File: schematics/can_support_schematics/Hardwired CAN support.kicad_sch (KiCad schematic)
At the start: 35 parts, among them J1 Conn_01x05_Female, J2 Conn_01x05_Male, J3 Conn_01x05_Male, J4 Screw_Terminal_01x04, J5 Screw_Terminal_01x02, J6 Screw_Terminal_01x02, J7 Screw_Terminal_01x02, Q1 MMBF170, SW1 SW_DIP_x04, U1 SPST_POWER_RELAY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

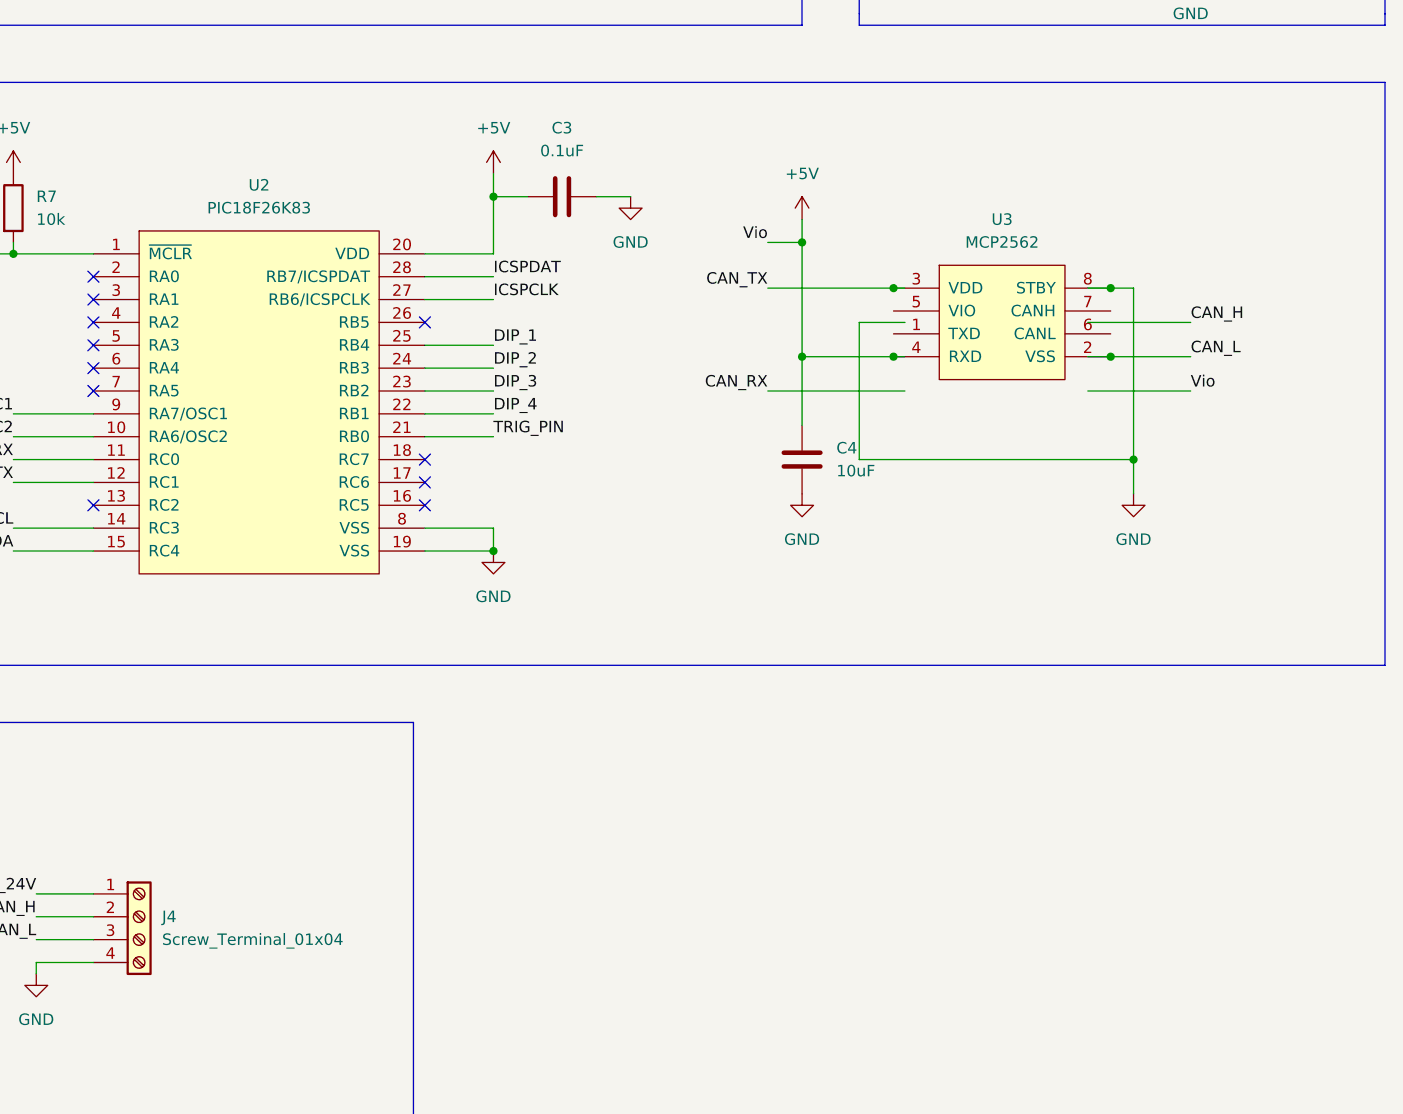
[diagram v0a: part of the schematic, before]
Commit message: Fixed CAN transceiver
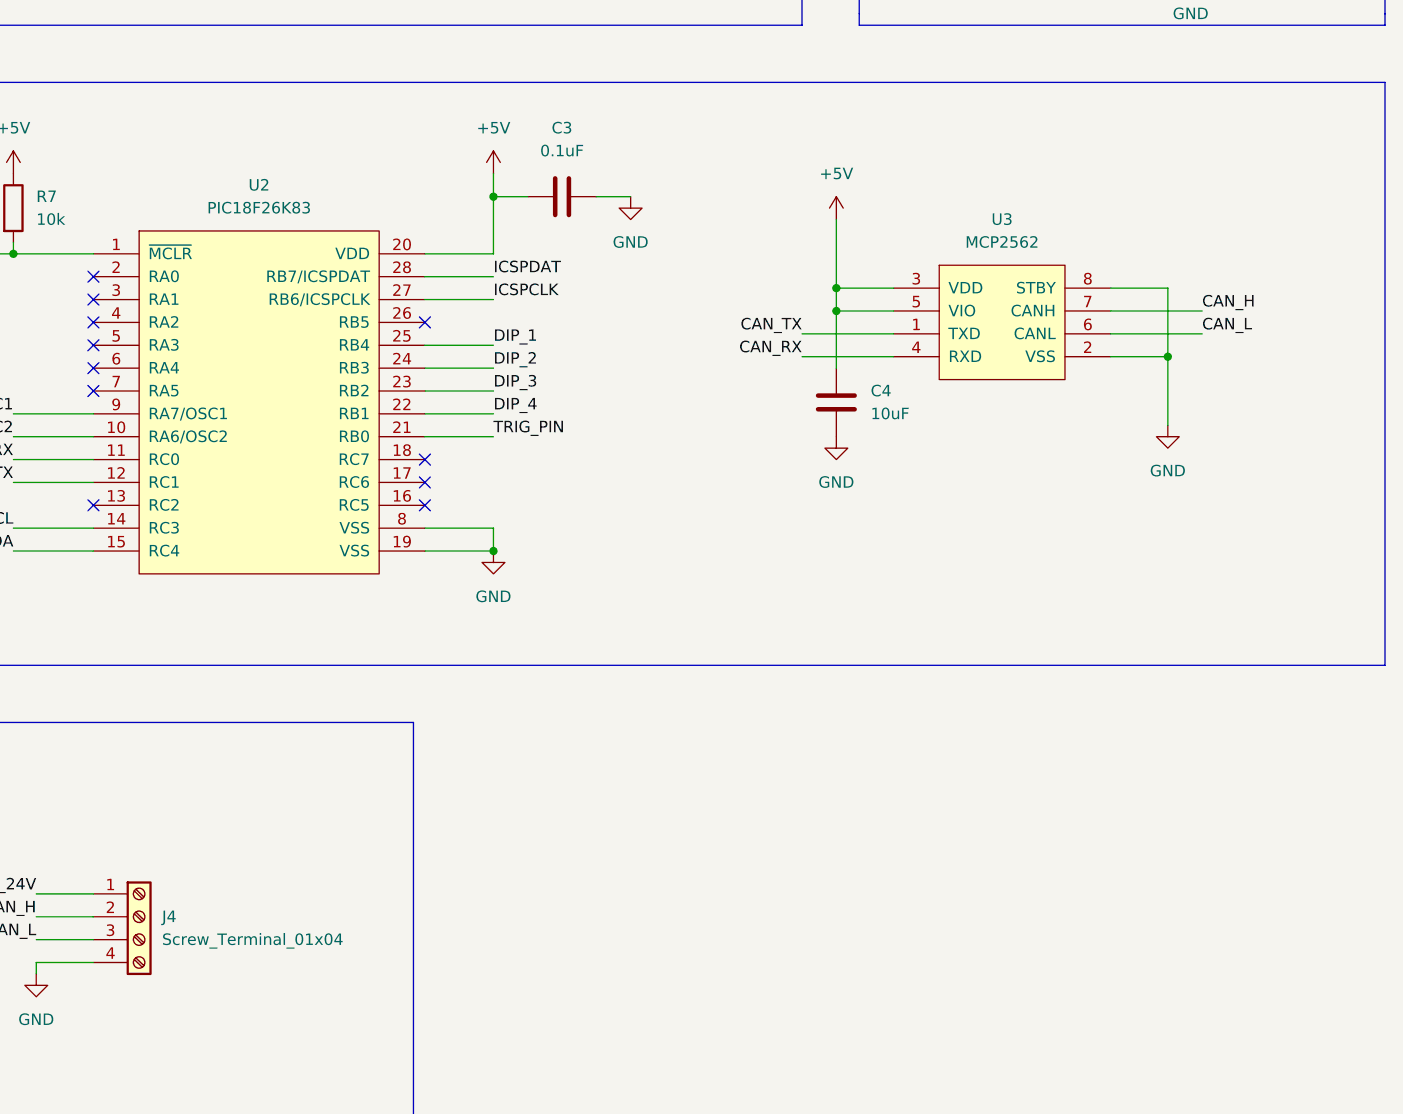
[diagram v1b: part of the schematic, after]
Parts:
- C4: footprint Capacitor_SMD:C_0805_2012Metric_Pad1.18x1.45mm_HandSolder -> (none)
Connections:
- net +5V: now also U3.3 (VDD), U3.5 (VIO); no longer U3.4 (RXD)
- net CAN_H: now also U3.7 (CANH)
- net CAN_L: now also U3.6 (CANL); no longer U3.2 (VSS)
- net CAN_RX: now also U3.4 (RXD)
- net CAN_TX: now also U3.1 (TXD); no longer U3.3 (VDD)
- net GND: now also U3.2 (VSS)

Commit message: Layout for PCB Plz Check and other updates
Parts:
- C4: footprint (none) -> Capacitor_SMD:C_0805_2012Metric_Pad1.18x1.45mm_HandSolder
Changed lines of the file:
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@@
       (effects (font (size 1.27 1.27)) (justify left))
     )
-    (property "Footprint" "" (id 2) (at 218.1352 104.14 0)
+    (property "Footprint" "Capacitor_SMD:C_0805_2012Metric_Pad1.18x1.45mm_HandSolder" (id 2) (at 218.1352 104.14 0)
       (effects (font (size 1.27 1.27)) hide)
     )
@@
     )
     (path "/d85f2563-6057-4c63-b8bd-55bd96b3561a"
-      (reference "C4") (unit 1) (value "10uF") (footprint "")
+      (reference "C4") (unit 1) (value "10uF") (footprint "Capacitor_SMD:C_0805_2012Metric_Pad1.18x1.45mm_HandSolder")
     )
     (path "/cb5f6738-8708-448f-b483-2bb4d72a4e96"

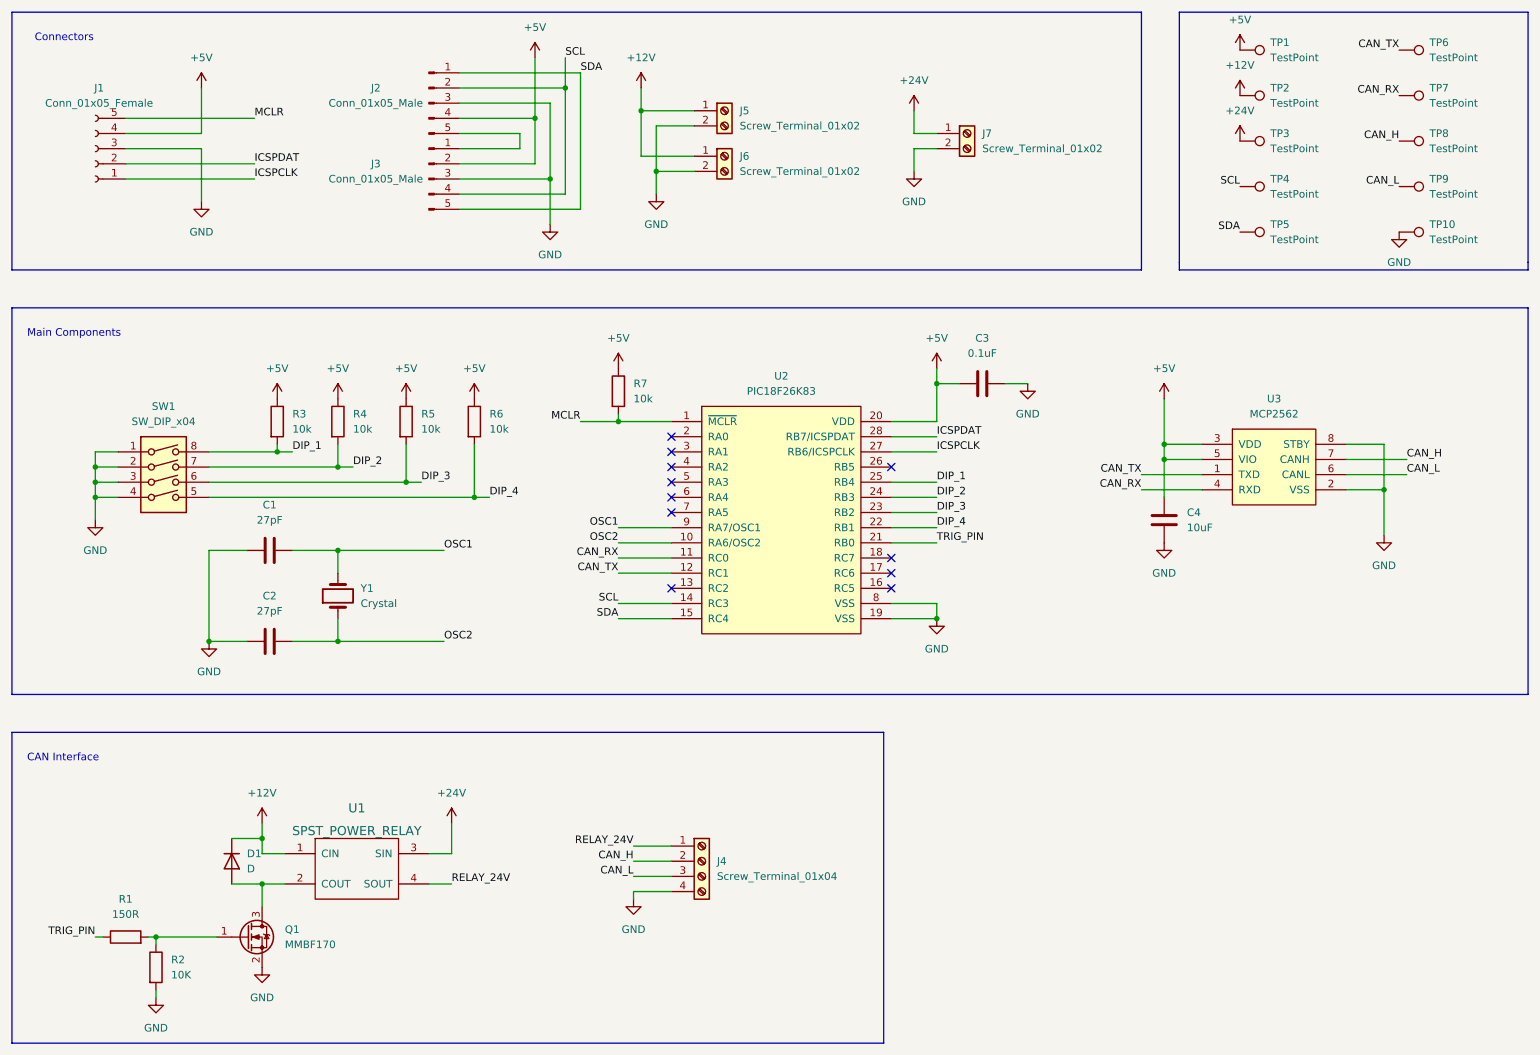
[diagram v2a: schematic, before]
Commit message: Finished routing board
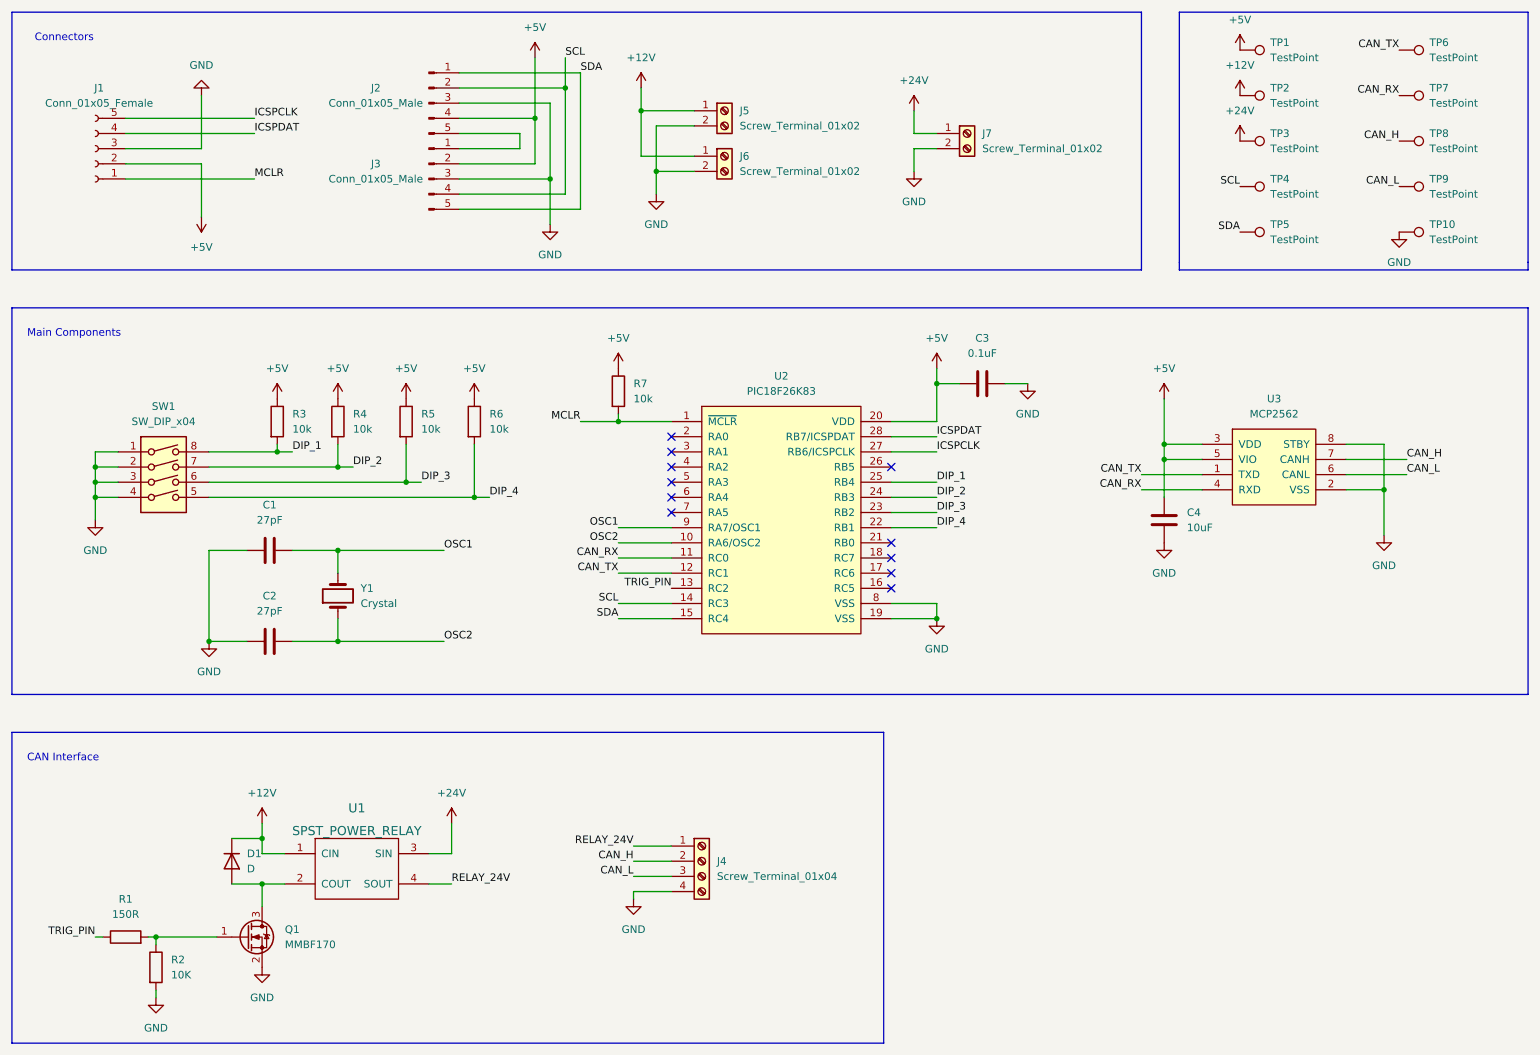
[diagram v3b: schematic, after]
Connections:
- net +5V: now also J1.2 (Pin_2); no longer J1.4 (Pin_4)
- net ICSPCLK: now also J1.5 (Pin_5); no longer J1.1 (Pin_1)
- net ICSPDAT: now also J1.4 (Pin_4); no longer J1.2 (Pin_2)
- net MCLR: now also J1.1 (Pin_1); no longer J1.5 (Pin_5)
- net TRIG_PIN: now also U2.13 (RC2); no longer U2.21 (RB0)
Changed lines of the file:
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@@
   (junction (at 101.6 96.52) (diameter 0) (color 0 0 0 0)
   )
-  (no_connect (at 134.62 111.76))
   (no_connect (at 171.45 106.68))
   (no_connect (at 171.45 111.76))
@@
   (no_connect (at 134.62 99.06))
   (no_connect (at 134.62 96.52))
+  (no_connect (at 171.45 104.14))
   (wire (pts (xy 111.76 40.64) (xy 99.06 40.64))
     (stroke (width 0) (type default) (color 0 0 0 0))
@@
     (stroke (width 0) (type default) (color 0 0 0 0))
   )
-  (wire (pts (xy 43.18 35.56) (xy 55.88 35.56))
+  (wire (pts (xy 43.18 35.56) (xy 64.77 35.56))
     (stroke (width 0) (type default) (color 0 0 0 0))
   )
@@
     (stroke (width 0) (type default) (color 0 0 0 0))
   )
+  (wire (pts (xy 55.88 29.21) (xy 55.88 38.1))
+    (stroke (width 0) (type default) (color 0 0 0 0))
+  )
   (wire (pts (xy 132.08 41.91) (xy 132.08 45.72))
     (stroke (width 0) (type default) (color 0 0 0 0))
@@
     (stroke (width 0) (type default) (color 0 0 0 0))
   )
-  (wire (pts (xy 55.88 38.1) (xy 55.88 46.99))
-    (stroke (width 0) (type default) (color 0 0 0 0))
-  )
   (wire (pts (xy 66.04 161.29) (xy 66.04 165.1))
     (stroke (width 0) (type default) (color 0 0 0 0))
@@
     (stroke (width 0) (type default) (color 0 0 0 0))
   )
-  (wire (pts (xy 55.88 27.94) (xy 55.88 35.56))
-    (stroke (width 0) (type default) (color 0 0 0 0))
-  )
   (wire (pts (xy 171.45 116.84) (xy 179.07 116.84))
     (stroke (width 0) (type default) (color 0 0 0 0))
@@
     (stroke (width 0) (type default) (color 0 0 0 0))
   )
-  (wire (pts (xy 43.18 40.64) (xy 64.77 40.64))
+  (wire (pts (xy 43.18 40.64) (xy 55.88 40.64))
     (stroke (width 0) (type default) (color 0 0 0 0))
   )
@@
     (stroke (width 0) (type default) (color 0 0 0 0))
   )
-  (wire (pts (xy 171.45 104.14) (xy 179.07 104.14))
-    (stroke (width 0) (type default) (color 0 0 0 0))
-  )
   (wire (pts (xy 171.45 88.9) (xy 179.07 88.9))
     (stroke (width 0) (type default) (color 0 0 0 0))
@@
     (stroke (width 0) (type default) (color 0 0 0 0))
   )
+  (wire (pts (xy 55.88 40.64) (xy 55.88 49.53))
+    (stroke (width 0) (type default) (color 0 0 0 0))
+  )
   (wire (pts (xy 71.12 105.41) (xy 78.74 105.41))
     (stroke (width 0) (type default) (color 0 0 0 0))
@@
     (effects (font (size 1.27 1.27)) (justify right bottom))
   )
+  (label "TRIG_PIN" (at 134.62 111.76 180)
+    (effects (font (size 1.27 1.27)) (justify right bottom))
+  )
   (label "CAN_L" (at 257.81 92.71 0)
     (effects (font (size 1.27 1.27)) (justify left bottom))
   )
-  (label "MCLR" (at 64.77 33.02 0)
-    (effects (font (size 1.27 1.27)) (justify left bottom))
-  )
-  (label "ICSPDAT" (at 64.77 40.64 0)
-    (effects (font (size 1.27 1.27)) (justify left bottom))
-  )
-  (label "TRIG_PIN" (at 179.07 104.14 0)
+  (label "MCLR" (at 64.77 43.18 0)
     (effects (font (size 1.27 1.27)) (justify left bottom))
   )
@@
     (effects (font (size 1.27 1.27)) (justify right bottom))
   )
-  (label "ICSPCLK" (at 64.77 43.18 0)
-    (effects (font (size 1.27 1.27)) (justify left bottom))
-  )
   (label "DIP_1" (at 179.07 93.98 0)
     (effects (font (size 1.27 1.27)) (justify left bottom))
@@
     (effects (font (size 1.27 1.27)) (justify right bottom))
   )
+  (label "ICSPDAT" (at 64.77 35.56 0)
+    (effects (font (size 1.27 1.27)) (justify left bottom))
+  )
   (label "DIP_4" (at 104.14 96.52 0)
     (effects (font (size 1.27 1.27)) (justify left bottom))
@@
   )
   (label "RELAY_24V" (at 97.79 161.29 0)
+    (effects (font (size 1.27 1.27)) (justify left bottom))
+  )
+  (label "ICSPCLK" (at 64.77 33.02 0)
     (effects (font (size 1.27 1.27)) (justify left bottom))
   )
@@
     (pin "1")
   )
+  (symbol (lib_id "power:GND") (at 55.88 29.21 180) (unit 1)
+    (in_bom yes) (on_board yes) (fields_autoplaced)
+    (property "Reference" "#PWR0106" (id 0) (at 55.88 22.86 0)
+      (effects (font (size 1.27 1.27)) hide)
+    )
+    (property "Value" "GND" (id 1) (at 55.88 24.13 0))
+    (property "Footprint" "" (id 2) (at 55.88 29.21 0)
+      (effects (font (size 1.27 1.27)) hide)
+    )
+    (property "Datasheet" "" (id 3) (at 55.88 29.21 0)
+      (effects (font (size 1.27 1.27)) hide)
+    )
+    (pin "1")
+  )
   (symbol (lib_id "power:+12V") (at 229.87 29.21 0) (unit 1)
     (in_bom yes) (on_board yes) (fields_autoplaced)
@@
     )
     (property "Datasheet" "" (id 3) (at 66.04 175.26 0)
-      (effects (font (size 1.27 1.27)) hide)
-    )
-    (pin "1")
-  )
-  (symbol (lib_id "power:GND") (at 55.88 46.99 0) (unit 1)
-    (in_bom yes) (on_board yes) (fields_autoplaced)
-    (property "Reference" "#PWR04" (id 0) (at 55.88 53.34 0)
-      (effects (font (size 1.27 1.27)) hide)
-    )
-    (property "Value" "GND" (id 1) (at 55.88 52.07 0))
-    (property "Footprint" "" (id 2) (at 55.88 46.99 0)
-      (effects (font (size 1.27 1.27)) hide)
-    )
-    (property "Datasheet" "" (id 3) (at 55.88 46.99 0)
       (effects (font (size 1.27 1.27)) hide)
     )
@@
     )
     (property "Datasheet" "" (id 3) (at 125.73 74.93 0)
+      (effects (font (size 1.27 1.27)) hide)
+    )
+    (pin "1")
+  )
+  (symbol (lib_id "power:+5V") (at 55.88 49.53 180) (unit 1)
+    (in_bom yes) (on_board yes) (fields_autoplaced)
+    (property "Reference" "#PWR0105" (id 0) (at 55.88 45.72 0)
+      (effects (font (size 1.27 1.27)) hide)
+    )
+    (property "Value" "+5V" (id 1) (at 55.88 54.61 0))
+    (property "Footprint" "" (id 2) (at 55.88 49.53 0)
+      (effects (font (size 1.27 1.27)) hide)
+    )
+    (property "Datasheet" "" (id 3) (at 55.88 49.53 0)
       (effects (font (size 1.27 1.27)) hide)
     )
@@
     (pin "1")
   )
-  (symbol (lib_id "power:+5V") (at 55.88 27.94 0) (unit 1)
-    (in_bom yes) (on_board yes) (fields_autoplaced)
-    (property "Reference" "#PWR03" (id 0) (at 55.88 31.75 0)
-      (effects (font (size 1.27 1.27)) hide)
-    )
-    (property "Value" "+5V" (id 1) (at 55.88 22.86 0))
-    (property "Footprint" "" (id 2) (at 55.88 27.94 0)
-      (effects (font (size 1.27 1.27)) hide)
-    )
-    (property "Datasheet" "" (id 3) (at 55.88 27.94 0)
-      (effects (font (size 1.27 1.27)) hide)
-    )
-    (pin "1")
-  )
   (symbol (lib_id "Connector:TestPoint") (at 256.54 29.21 270) (unit 1)
     (in_bom yes) (on_board yes) (fields_autoplaced)
@@
       (reference "#PWR02") (unit 1) (value "+5V") (footprint "")
     )
-    (path "/fc3e498d-d0cd-4c1a-a2fe-632568988592"
-      (reference "#PWR03") (unit 1) (value "+5V") (footprint "")
-    )
-    (path "/7d654e39-30f5-4364-b45a-95a72d3c3ee4"
-      (reference "#PWR04") (unit 1) (value "GND") (footprint "")
-    )
     (path "/705e8294-3269-44a7-a117-43cc65252d68"
       (reference "#PWR05") (unit 1) (value "GND") (footprint "")
@@
       (reference "#PWR0104") (unit 1) (value "+24V") (footprint "")
     )
+    (path "/c91b8104-1c96-4bf2-b6fb-8bdf8adbf6c6"
+      (reference "#PWR0105") (unit 1) (value "+5V") (footprint "")
+    )
+    (path "/6ba02eba-914c-45a1-b69c-35b19e165048"
+      (reference "#PWR0106") (unit 1) (value "GND") (footprint "")
+    )
     (path "/e3df130c-26dc-4141-abb6-87ca871717b3"
